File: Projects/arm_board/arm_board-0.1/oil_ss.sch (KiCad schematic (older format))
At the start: 1 part

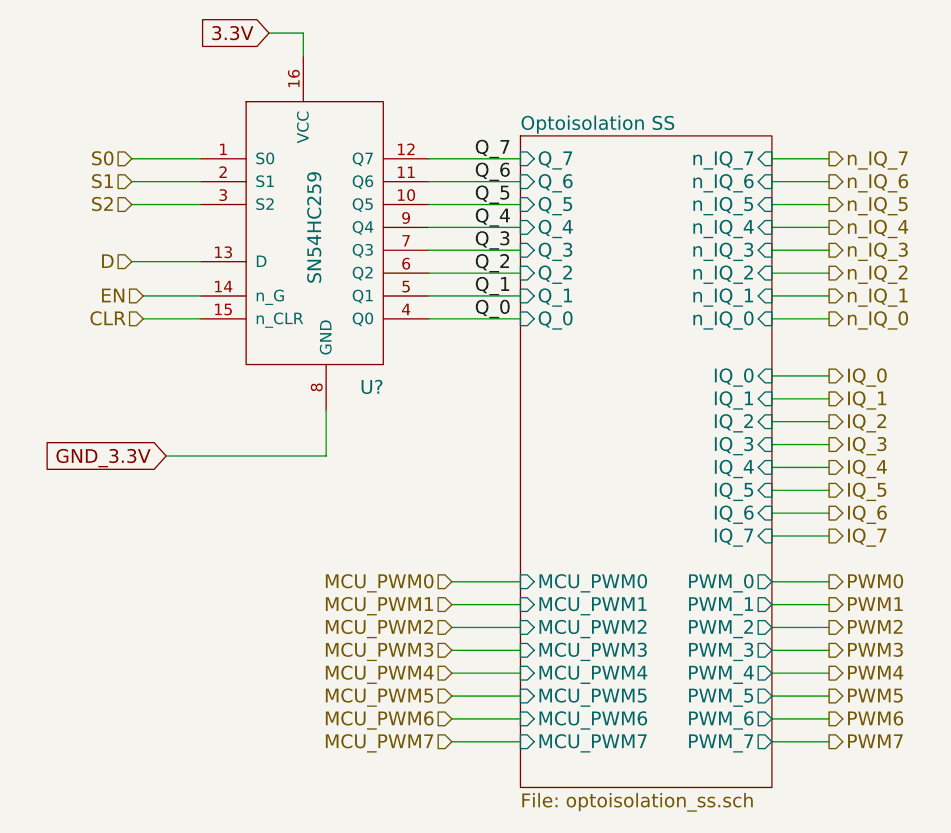
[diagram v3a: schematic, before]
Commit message: Arm Board: bug fixes, and added footprints
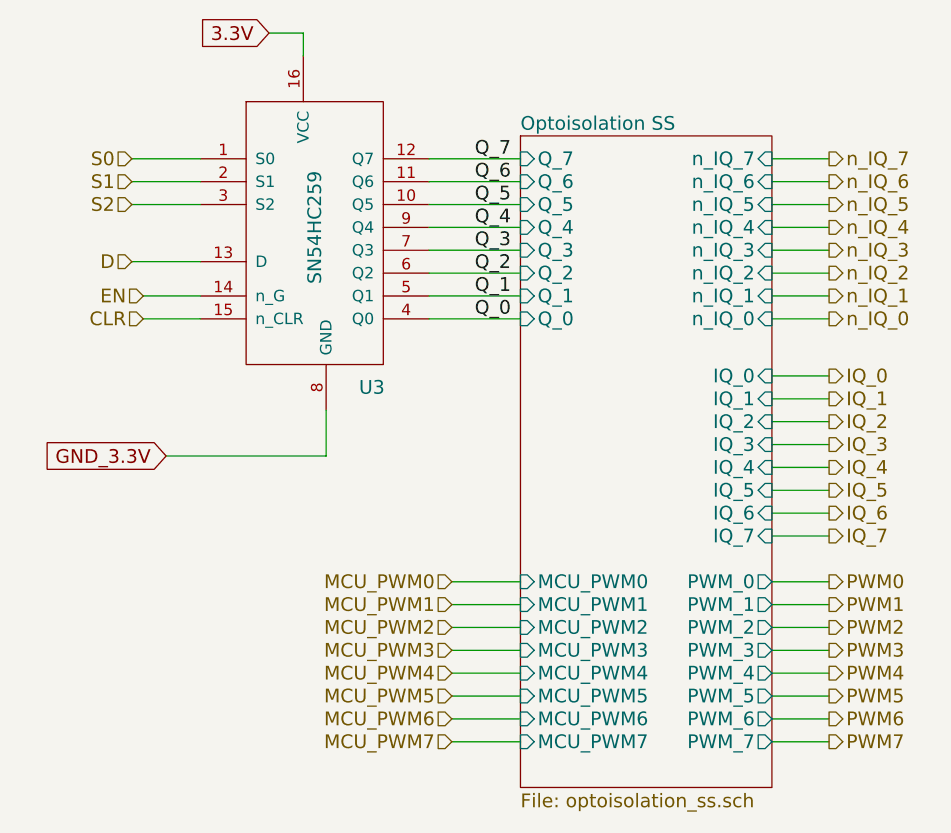
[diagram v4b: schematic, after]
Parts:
- U3: renamed from U?; footprint (none) -> SMD_Packages:SO-16-N
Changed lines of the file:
@@
 LIBS:ArmComponentLibrary
 LIBS:arm_board-cache
-EELAYER 27 0
+EELAYER 25 0
 EELAYER END
 $Descr A4 11693 8268
@@
 IQ_7
 $Comp
-L SN54HC259 U?
+L SN54HC259 U3
 U 1 1 5660DAA6
 P 3700 2000
-F 0 "U?" H 3950 1350 60  0000 C CNN
+F 0 "U3" H 3950 1350 60  0000 C CNN
 F 1 "SN54HC259" V 3700 2050 60  0000 C CNN
-F 2 "" H 3700 1900 60  0000 C CNN
+F 2 "SMD_Packages:SO-16-N" H 3700 1900 60  0001 C CNN
 F 3 "" H 3700 1900 60  0000 C CNN
 	1    3700 2000

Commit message: Arm Board: finalizing footprints.
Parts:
- U3: footprint SMD_Packages:SO-16-N -> ArmFootprints:SOIC-16
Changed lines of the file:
@@
 F 0 "U3" H 3950 1350 60  0000 C CNN
 F 1 "SN54HC259" V 3700 2050 60  0000 C CNN
-F 2 "SMD_Packages:SO-16-N" H 3700 1900 60  0001 C CNN
+F 2 "ArmFootprints:SOIC-16" H 3700 1900 60  0001 C CNN
 F 3 "" H 3700 1900 60  0000 C CNN
 	1    3700 2000
